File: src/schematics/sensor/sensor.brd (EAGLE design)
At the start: 50.8 x 35.6 mm, 10 parts

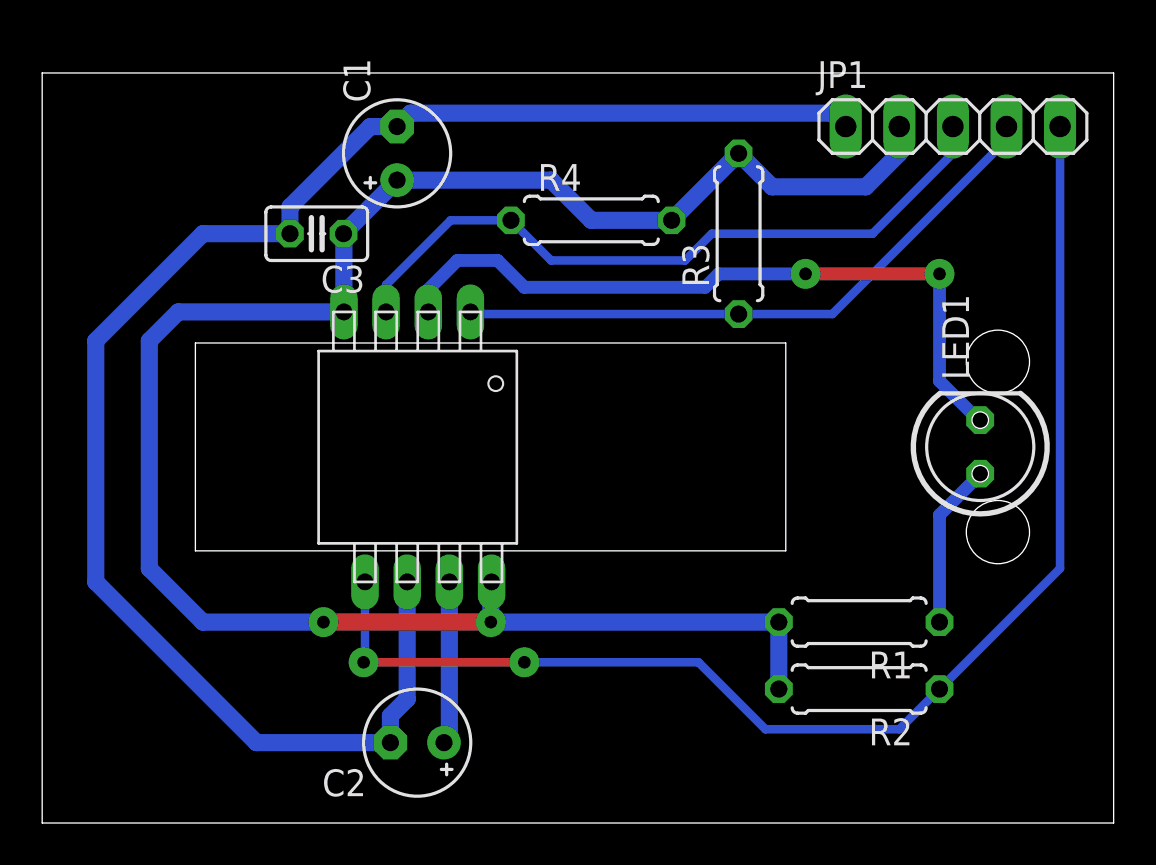
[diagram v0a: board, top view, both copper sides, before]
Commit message: Sensor PCB updates
Minor changes to the sensor module PCB layout.

Andrea Zoppi
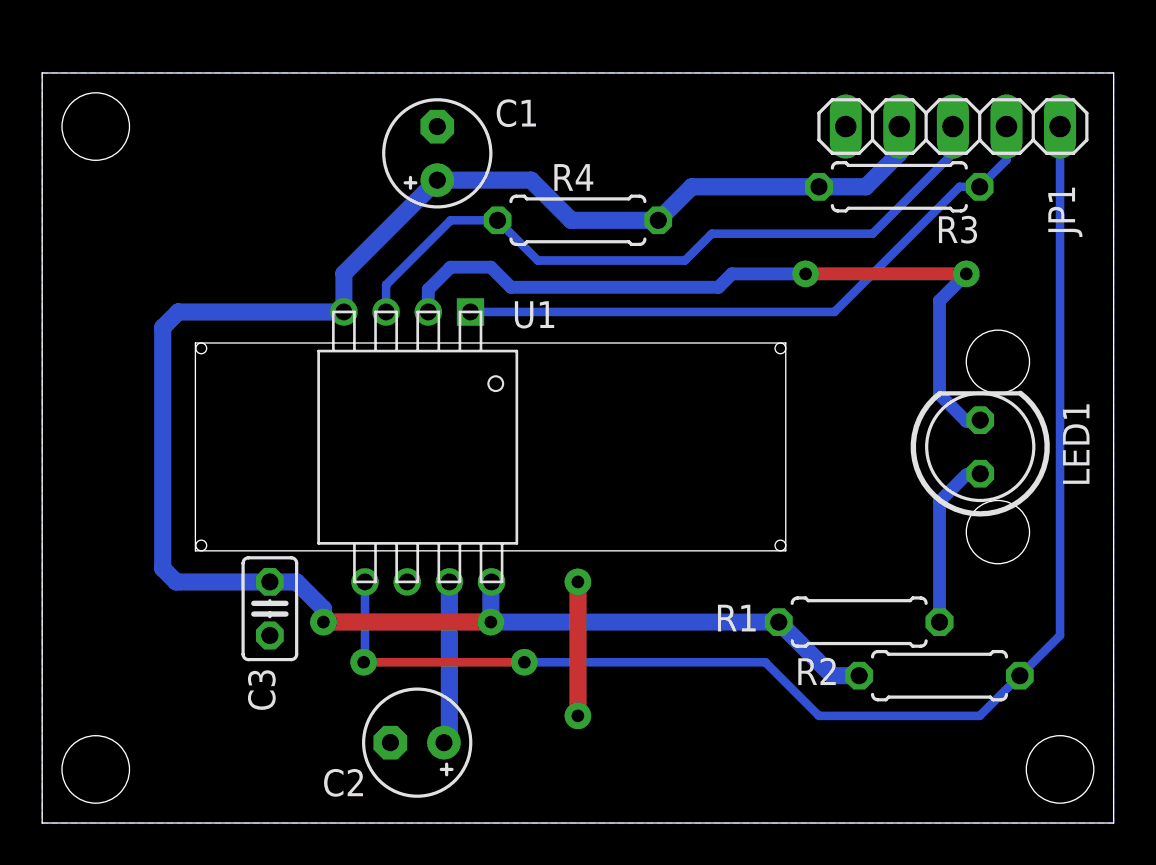
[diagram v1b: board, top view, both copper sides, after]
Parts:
- R1: value 66 -> 68
- moved C3 17.9 mm to (10.8, 10.2), turned to 270 degrees
- moved R3 7.94 mm to (40.6, 30.2), turned to 180 degrees
- moved R2 3.86 mm to (42.5, 6.99)
- moved C1 1.91 mm to (18.7, 31.8)
- moved R4 0.64 mm to (25.4, 28.6)
- renumbered U$1 to U1
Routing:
- net GND: track 77.5 -> 6.35 mm, vias 0 -> 2
- net N$6: track 34.4 -> 36.3 mm
- net SCLK: track 62.3 -> 63.6 mm
- net +3V3: track 92.4 -> 91.1 mm
- net SDIO: track 29.5 -> 30.0 mm
- added copper zone on layer 16, net GND
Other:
- board text added: "1"
- board text added: "1 GND"
- board text added: "2 3V3"
- board text added: "3 MOTION"
- board text added: "4 SDIO"
- board text added: "5 SCLK"

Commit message: Minor PCB fixes
Changed resistor values so that performance is improved, and the PIC
inputs can read correct pull-up values.

Andrea Zoppi
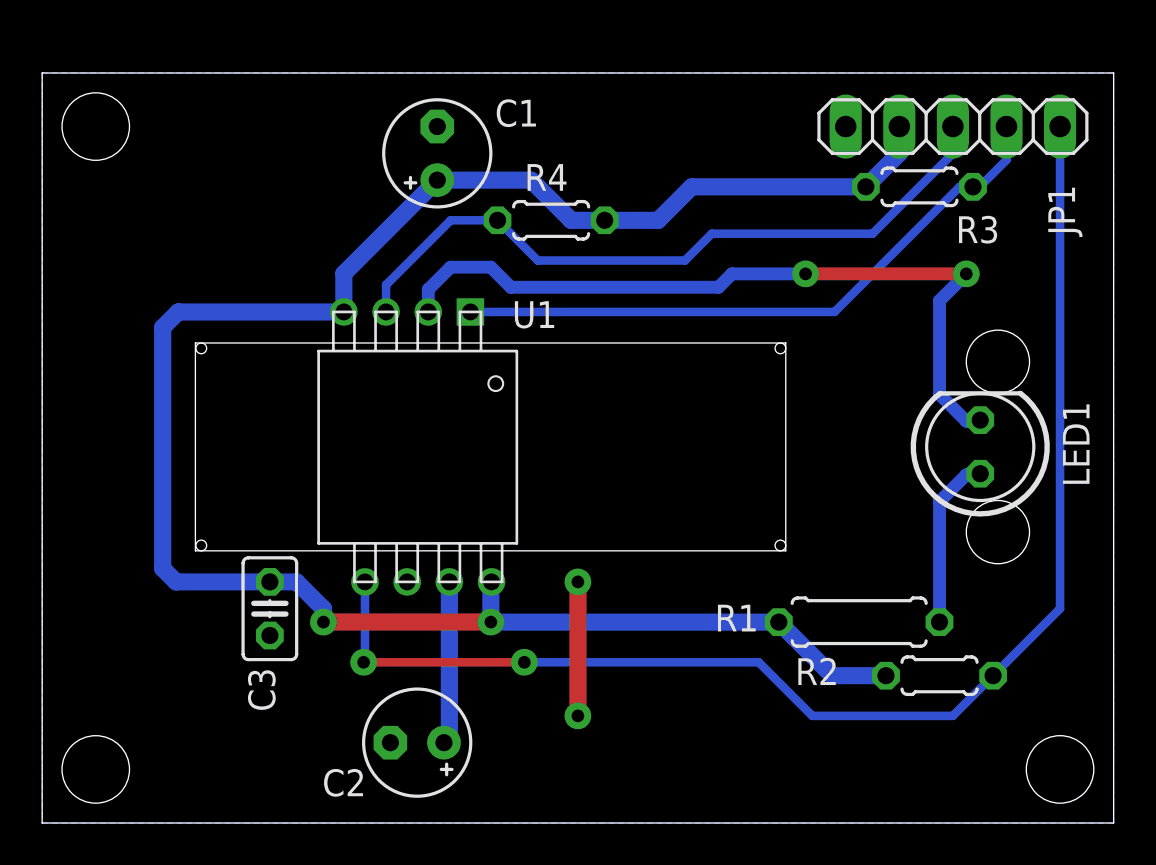
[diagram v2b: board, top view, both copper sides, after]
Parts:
- R2, R3, R4: value 1M -> 100k; device rcl:0207/7 -> rcl:0204/5
- moved R4 1.27 mm to (24.1, 28.6)
- moved R3 0.95 mm to (41.6, 30.2)
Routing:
- net +3V3: track 91.1 -> 92.4 mm
- net SCLK: track 63.6 -> 62.9 mm
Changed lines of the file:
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@@
 <attribute name="VALUE" x="46.2788" y="21.0312" size="1.27" layer="27" ratio="10" rot="R90"/>
 </element>
-<element name="R2" library="rcl" package="0207/7" value="1M" x="42.545" y="6.985" smashed="yes" rot="R180">
+<element name="R2" library="rcl" package="0204/5" value="100k" x="42.545" y="6.985" smashed="yes" rot="R180">
 <attribute name="NAME" x="37.7825" y="7.8105" size="1.27" layer="25" ratio="10" rot="R180"/>
 </element>
-<element name="R3" library="rcl" package="0207/7" value="1M" x="40.64" y="30.1625" smashed="yes" rot="R180">
-<attribute name="NAME" x="44.45" y="28.7655" size="1.27" layer="25" ratio="10" rot="R180"/>
+<element name="R3" library="rcl" package="0204/5" value="100k" x="41.5925" y="30.1625" smashed="yes" rot="R180">
+<attribute name="NAME" x="45.4025" y="28.7655" size="1.27" layer="25" ratio="10" rot="R180"/>
 </element>
-<element name="R4" library="rcl" package="0207/7" value="1M" x="25.4" y="28.575" smashed="yes">
-<attribute name="NAME" x="24.13" y="29.972" size="1.27" layer="25" ratio="10"/>
+<element name="R4" library="rcl" package="0204/5" value="100k" x="24.13" y="28.575" smashed="yes">
+<attribute name="NAME" x="22.86" y="29.972" size="1.27" layer="25" ratio="10"/>
 </element>
 </elements>
@@
 <wire x1="39.0525" y1="30.1625" x2="30.7975" y2="30.1625" width="0.8128" layer="16"/>
 <wire x1="34.925" y1="9.525" x2="37.465" y2="6.985" width="0.8128" layer="16"/>
-<wire x1="37.465" y1="6.985" x2="38.735" y2="6.985" width="0.8128" layer="16"/>
-<wire x1="29.21" y1="28.575" x2="25.0825" y2="28.575" width="0.8128" layer="16"/>
+<wire x1="37.465" y1="6.985" x2="40.005" y2="6.985" width="0.8128" layer="16"/>
+<wire x1="26.67" y1="28.575" x2="25.0825" y2="28.575" width="0.8128" layer="16"/>
 <wire x1="25.0825" y1="28.575" x2="23.1775" y2="30.48" width="0.8128" layer="16"/>
 <wire x1="23.1775" y1="30.48" x2="18.7325" y2="30.48" width="0.8128" layer="16"/>
@@
 <wire x1="13.335" y1="10.16" x2="13.335" y2="9.525" width="0.8128" layer="16"/>
 <wire x1="30.7975" y1="30.1625" x2="29.21" y2="28.575" width="0.8128" layer="16"/>
-<wire x1="39.0525" y1="30.1625" x2="36.83" y2="30.1625" width="0" layer="19" extent="16-16"/>
+<wire x1="29.21" y1="28.575" x2="26.67" y2="28.575" width="0.8128" layer="16"/>
 </signal>
 <signal name="N$2">
@@
 <wire x1="45.72" y1="33.02" x2="45.72" y2="31.4325" width="0.4064" layer="16"/>
 <wire x1="45.72" y1="31.4325" x2="44.45" y2="30.1625" width="0.4064" layer="16"/>
+<wire x1="44.45" y1="30.1625" x2="44.1325" y2="30.1625" width="0.4064" layer="16"/>
 <wire x1="20.3054" y1="24.2308" x2="37.5658" y2="24.2308" width="0.4064" layer="16"/>
 <wire x1="37.5658" y1="24.2308" x2="43.4975" y2="30.1625" width="0.4064" layer="16"/>
-<wire x1="43.4975" y1="30.1625" x2="44.45" y2="30.1625" width="0.4064" layer="16"/>
+<wire x1="43.4975" y1="30.1625" x2="44.1325" y2="30.1625" width="0.4064" layer="16"/>
 </signal>
 <signal name="SCLK">
@@
 <contactref element="U1" pad="5"/>
 <contactref element="R2" pad="1"/>
-<wire x1="48.26" y1="33.02" x2="48.26" y2="8.89" width="0.4064" layer="16"/>
-<wire x1="48.26" y1="8.89" x2="46.355" y2="6.985" width="0.4064" layer="16"/>
+<wire x1="48.26" y1="33.02" x2="48.26" y2="10.16" width="0.4064" layer="16"/>
+<wire x1="48.26" y1="10.16" x2="45.085" y2="6.985" width="0.4064" layer="16"/>
 <wire x1="15.3054" y1="7.6854" x2="15.24" y2="7.62" width="0.4064" layer="16"/>
 <via x="15.24" y="7.62" extent="1-16" drill="0.6" diameter="1.27" shape="octagon"/>
 <wire x1="15.24" y1="7.62" x2="22.86" y2="7.62" width="0.4064" layer="1"/>
 <via x="22.86" y="7.62" extent="1-16" drill="0.6" diameter="1.27" shape="octagon"/>
-<wire x1="46.355" y1="6.985" x2="44.45" y2="5.08" width="0.4064" layer="16"/>
-<wire x1="44.45" y1="5.08" x2="36.83" y2="5.08" width="0.4064" layer="16"/>
-<wire x1="36.83" y1="5.08" x2="34.29" y2="7.62" width="0.4064" layer="16"/>
-<wire x1="34.29" y1="7.62" x2="22.86" y2="7.62" width="0.4064" layer="16"/>
+<wire x1="45.085" y1="6.985" x2="43.18" y2="5.08" width="0.4064" layer="16"/>
+<wire x1="43.18" y1="5.08" x2="36.5125" y2="5.08" width="0.4064" layer="16"/>
+<wire x1="36.5125" y1="5.08" x2="33.9725" y2="7.62" width="0.4064" layer="16"/>
+<wire x1="33.9725" y1="7.62" x2="22.86" y2="7.62" width="0.4064" layer="16"/>
 <wire x1="15.3054" y1="11.4308" x2="15.3054" y2="7.6854" width="0.4064" layer="16"/>
 </signal>

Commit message: Fixed PCB libraries
Some components in the extended Microxhip library had wrong dual-in-line
package drawings.

The libraries were renamed as "local" instead of "extended".

Minor fixes in both schematics and PCBs.

Andrea Zoppi
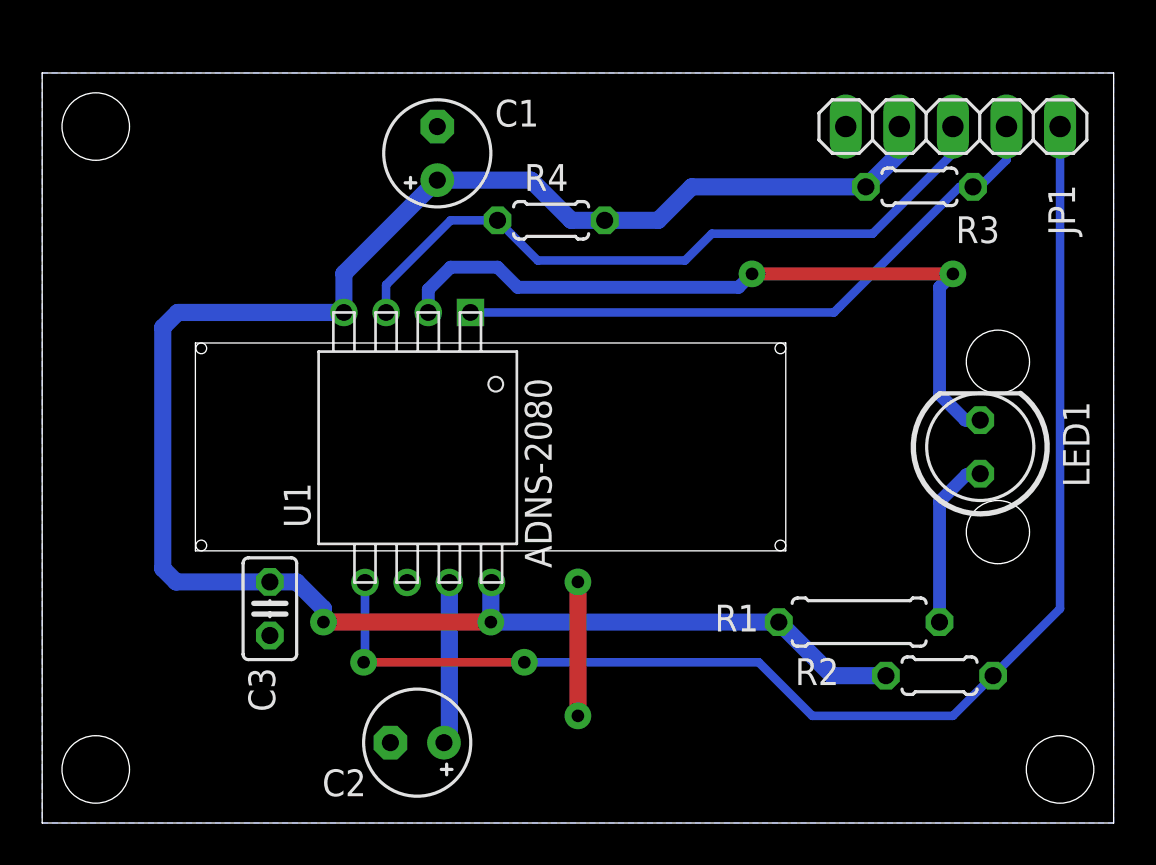
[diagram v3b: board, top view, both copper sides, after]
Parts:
- U1: device avago_extended:DIP8-OPTICAL -> avago_local:DIP8-OPTICAL
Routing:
- net N$6: track 36.3 -> 35.5 mm
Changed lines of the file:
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@@
 </autorouter>
 <elements>
-<element name="U1" library="avago_extended" package="DIP8-OPTICAL" value="ADNS-2080" x="17.8054" y="17.8308" locked="yes" smashed="yes" rot="R90">
-<attribute name="NAME" x="22.2758" y="23.4696" size="1.27" layer="21"/>
-</element>
 <element name="JP1" library="pinhead" package="1X05" value="" x="43.18" y="33.02" locked="yes" smashed="yes">
 <attribute name="NAME" x="48.9712" y="27.8638" size="1.27" layer="25" ratio="10" rot="R90"/>
@@
 <attribute name="NAME" x="22.86" y="29.972" size="1.27" layer="25" ratio="10"/>
 </element>
+<element name="U1" library="avago_local" package="DIP8-OPTICAL" value="ADNS-2080" x="17.8054" y="17.8054" rot="R90"/>
 </elements>
 <signals>
 <signal name="+3V3">
-<contactref element="U1" pad="4"/>
 <contactref element="C1" pad="+"/>
 <contactref element="C3" pad="1"/>
-<contactref element="U1" pad="8"/>
 <contactref element="R1" pad="2"/>
 <contactref element="JP1" pad="2"/>
@@
 <wire x1="25.0825" y1="28.575" x2="23.1775" y2="30.48" width="0.8128" layer="16"/>
 <wire x1="23.1775" y1="30.48" x2="18.7325" y2="30.48" width="0.8128" layer="16"/>
-<wire x1="14.3054" y1="24.2308" x2="6.4508" y2="24.2308" width="0.8128" layer="16"/>
-<wire x1="6.4508" y1="24.2308" x2="5.715" y2="23.495" width="0.8128" layer="16"/>
 <wire x1="5.715" y1="23.495" x2="5.715" y2="12.065" width="0.8128" layer="16"/>
 <wire x1="5.715" y1="12.065" x2="6.35" y2="11.43" width="0.8128" layer="16"/>
@@
 <via x="21.2725" y="9.525" extent="1-16" drill="0.6" diameter="1.27" shape="octagon"/>
 <wire x1="21.2725" y1="9.525" x2="21.2725" y2="11.3979" width="0.8128" layer="16"/>
-<wire x1="21.2725" y1="11.3979" x2="21.3054" y2="11.4308" width="0.8128" layer="16"/>
 <wire x1="34.925" y1="9.525" x2="21.2725" y2="9.525" width="0.8128" layer="16"/>
-<wire x1="14.3054" y1="24.2308" x2="14.3054" y2="26.0529" width="0.8128" layer="16"/>
 <wire x1="14.3054" y1="26.0529" x2="18.7325" y2="30.48" width="0.8128" layer="16"/>
 <wire x1="10.795" y1="11.43" x2="12.065" y2="11.43" width="0.8128" layer="16"/>
@@
 <wire x1="30.7975" y1="30.1625" x2="29.21" y2="28.575" width="0.8128" layer="16"/>
 <wire x1="29.21" y1="28.575" x2="26.67" y2="28.575" width="0.8128" layer="16"/>
+<contactref element="U1" pad="4"/>
+<contactref element="U1" pad="8"/>
+<wire x1="14.3054" y1="26.0529" x2="14.3054" y2="24.2054" width="0.8128" layer="16"/>
+<wire x1="14.3054" y1="24.2054" x2="6.4254" y2="24.2054" width="0.8128" layer="16"/>
+<wire x1="6.4254" y1="24.2054" x2="5.715" y2="23.495" width="0.8128" layer="16"/>
+<wire x1="21.2725" y1="11.3979" x2="21.3054" y2="11.4054" width="0" layer="19" extent="16-16"/>
 </signal>
 <signal name="N$2">
+<contactref element="C2" pad="+"/>
 <contactref element="U1" pad="7"/>
-<contactref element="C2" pad="+"/>
-<wire x1="19.3054" y1="11.4308" x2="19.3054" y2="4.0654" width="0.8128" layer="16"/>
+<wire x1="19.3054" y1="11.4054" x2="19.3054" y2="4.0654" width="0.8128" layer="16"/>
 <wire x1="19.3054" y1="4.0654" x2="19.05" y2="3.81" width="0.8128" layer="16"/>
 </signal>
@@
 <contactref element="C3" pad="2"/>
 <contactref element="C2" pad="-"/>
-<contactref element="U1" pad="6"/>
 <contactref element="JP1" pad="1"/>
 <polygon width="0.4064" layer="16">
@@
 <via x="25.4" y="11.43" extent="1-16" drill="0.6" diameter="1.27" shape="octagon"/>
 <via x="25.4" y="5.08" extent="1-16" drill="0.6" diameter="1.27" shape="octagon"/>
+<contactref element="U1" pad="6"/>
 </signal>
 <signal name="N$5">
@@
 <contactref element="LED1" pad="K"/>
 <contactref element="U1" pad="2"/>
-<wire x1="18.3054" y1="24.2308" x2="18.3054" y2="25.2904" width="0.6096" layer="16"/>
+<wire x1="44.4754" y1="19.1008" x2="43.7642" y2="19.1008" width="0.6096" layer="16"/>
+<wire x1="43.7642" y1="19.1008" x2="42.545" y2="20.32" width="0.6096" layer="16"/>
+<wire x1="42.545" y1="20.32" x2="42.545" y2="25.4" width="0.6096" layer="16"/>
+<wire x1="42.545" y1="25.4" x2="43.18" y2="26.035" width="0.6096" layer="16"/>
+<via x="43.18" y="26.035" extent="1-16" drill="0.6" diameter="1.27" shape="octagon"/>
+<wire x1="43.18" y1="26.035" x2="33.655" y2="26.035" width="0.6096" layer="1"/>
+<via x="33.655" y="26.035" extent="1-16" drill="0.6" diameter="1.27" shape="octagon"/>
+<wire x1="33.655" y1="26.035" x2="33.02" y2="25.4" width="0.6096" layer="16"/>
+<wire x1="33.02" y1="25.4" x2="22.5425" y2="25.4" width="0.6096" layer="16"/>
+<wire x1="22.5425" y1="25.4" x2="21.59" y2="26.3525" width="0.6096" layer="16"/>
+<wire x1="21.59" y1="26.3525" x2="19.3675" y2="26.3525" width="0.6096" layer="16"/>
+<wire x1="18.3054" y1="24.2054" x2="18.3054" y2="25.2904" width="0.6096" layer="16"/>
 <wire x1="18.3054" y1="25.2904" x2="19.3675" y2="26.3525" width="0.6096" layer="16"/>
-<wire x1="19.3675" y1="26.3525" x2="21.2725" y2="26.3525" width="0.6096" layer="16"/>
-<wire x1="21.2725" y1="26.3525" x2="22.225" y2="25.4" width="0.6096" layer="16"/>
-<wire x1="22.225" y1="25.4" x2="32.0675" y2="25.4" width="0.6096" layer="16"/>
-<wire x1="32.0675" y1="25.4" x2="32.7025" y2="26.035" width="0.6096" layer="16"/>
-<wire x1="32.7025" y1="26.035" x2="36.195" y2="26.035" width="0.6096" layer="16"/>
-<via x="36.195" y="26.035" extent="1-16" drill="0.6" diameter="1.27" shape="octagon"/>
-<wire x1="36.195" y1="26.035" x2="43.815" y2="26.035" width="0.6096" layer="1"/>
-<via x="43.815" y="26.035" extent="1-16" drill="0.6" diameter="1.27" shape="octagon"/>
-<wire x1="43.815" y1="26.035" x2="42.545" y2="24.765" width="0.6096" layer="16"/>
-<wire x1="42.545" y1="24.765" x2="42.545" y2="20.32" width="0.6096" layer="16"/>
-<wire x1="42.545" y1="20.32" x2="43.815" y2="19.05" width="0.6096" layer="16"/>
-<wire x1="43.815" y1="19.05" x2="44.45" y2="19.05" width="0.6096" layer="16"/>
-<wire x1="44.45" y1="19.05" x2="44.4754" y2="19.1008" width="0" layer="19" extent="16-16"/>
 </signal>
 <signal name="MOTION">
-<contactref element="U1" pad="3"/>
 <contactref element="JP1" pad="3"/>
 <contactref element="R4" pad="1"/>
@@
 <wire x1="39.37" y1="27.94" x2="43.18" y2="31.75" width="0.4064" layer="16"/>
 <wire x1="43.18" y1="31.75" x2="43.18" y2="33.02" width="0.4064" layer="16"/>
-<wire x1="16.3054" y1="24.2308" x2="16.3054" y2="25.5129" width="0.4064" layer="16"/>
 <wire x1="16.3054" y1="25.5129" x2="19.3675" y2="28.575" width="0.4064" layer="16"/>
 <wire x1="19.3675" y1="28.575" x2="21.59" y2="28.575" width="0.4064" layer="16"/>
 <wire x1="30.48" y1="26.67" x2="23.495" y2="26.67" width="0.4064" layer="16"/>
 <wire x1="23.495" y1="26.67" x2="21.59" y2="28.575" width="0.4064" layer="16"/>
+<contactref element="U1" pad="3"/>
+<wire x1="16.3054" y1="25.5129" x2="16.3054" y2="24.2054" width="0.4064" layer="16"/>
 </signal>
 <signal name="SDIO">
 <contactref element="JP1" pad="4"/>
-<contactref element="U1" pad="1"/>
 <contactref element="R3" pad="1"/>
 <wire x1="45.72" y1="33.02" x2="45.72" y2="31.4325" width="0.4064" layer="16"/>
 <wire x1="45.72" y1="31.4325" x2="44.45" y2="30.1625" width="0.4064" layer="16"/>
 <wire x1="44.45" y1="30.1625" x2="44.1325" y2="30.1625" width="0.4064" layer="16"/>
-<wire x1="20.3054" y1="24.2308" x2="37.5658" y2="24.2308" width="0.4064" layer="16"/>
-<wire x1="37.5658" y1="24.2308" x2="43.4975" y2="30.1625" width="0.4064" layer="16"/>
+<wire x1="37.5658" y1="24.2308" x2="37.7825" y2="24.4475" width="0.4064" layer="16"/>
+<wire x1="37.7825" y1="24.4475" x2="43.4975" y2="30.1625" width="0.4064" layer="16"/>
 <wire x1="43.4975" y1="30.1625" x2="44.1325" y2="30.1625" width="0.4064" layer="16"/>
+<contactref element="U1" pad="1"/>
+<wire x1="20.3054" y1="24.2054" x2="37.5404" y2="24.2054" width="0.4064" layer="16"/>
+<wire x1="37.5404" y1="24.2054" x2="37.5658" y2="24.2308" width="0.4064" layer="16"/>
 </signal>
 <signal name="SCLK">
 <contactref element="JP1" pad="5"/>
-<contactref element="U1" pad="5"/>
 <contactref element="R2" pad="1"/>
 <wire x1="48.26" y1="33.02" x2="48.26" y2="10.16" width="0.4064" layer="16"/>
 <wire x1="48.26" y1="10.16" x2="45.085" y2="6.985" width="0.4064" layer="16"/>
-<wire x1="15.3054" y1="7.6854" x2="15.24" y2="7.62" width="0.4064" layer="16"/>
 <via x="15.24" y="7.62" extent="1-16" drill="0.6" diameter="1.27" shape="octagon"/>
 <wire x1="15.24" y1="7.62" x2="22.86" y2="7.62" width="0.4064" layer="1"/>
@@
 <wire x1="36.5125" y1="5.08" x2="33.9725" y2="7.62" width="0.4064" layer="16"/>
 <wire x1="33.9725" y1="7.62" x2="22.86" y2="7.62" width="0.4064" layer="16"/>
-<wire x1="15.3054" y1="11.4308" x2="15.3054" y2="7.6854" width="0.4064" layer="16"/>
+<contactref element="U1" pad="5"/>
+<wire x1="15.3054" y1="11.4054" x2="15.3054" y2="7.6854" width="0.4064" layer="16"/>
+<wire x1="15.3054" y1="7.6854" x2="15.24" y2="7.62" width="0.4064" layer="16"/>
 </signal>
 </signals>
